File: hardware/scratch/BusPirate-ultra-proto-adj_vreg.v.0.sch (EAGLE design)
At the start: 18 parts, among them J1 CON_HEADER_1X02-PTH, J2 CON_HEADER_1X02-PTH, J3 CON_HEADER_1X02-PTH, Q1 DMMT3906W, Q3 FDS6575, U1 LM317T, U2 MCP6001

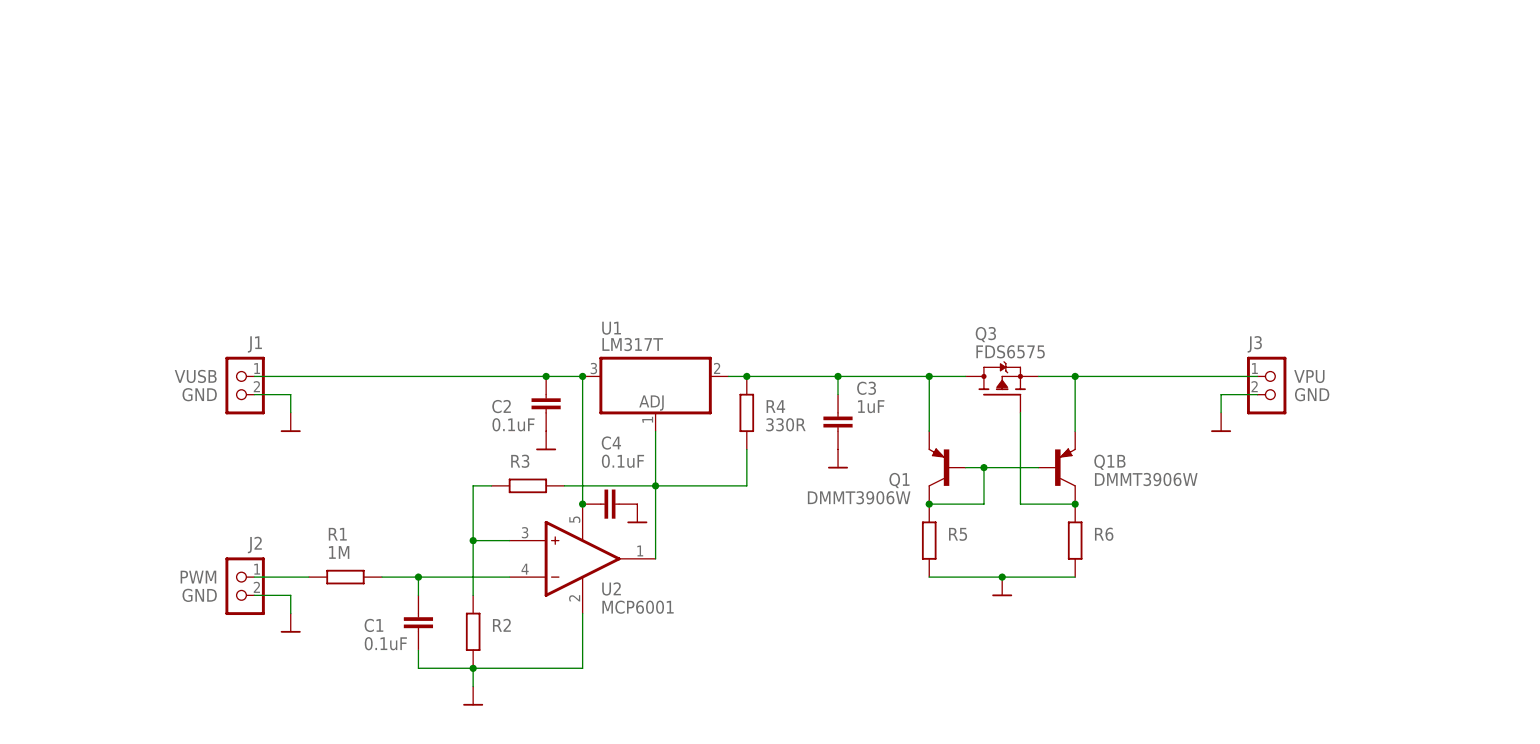
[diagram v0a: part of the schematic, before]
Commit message: changed vreg and pass mosfet
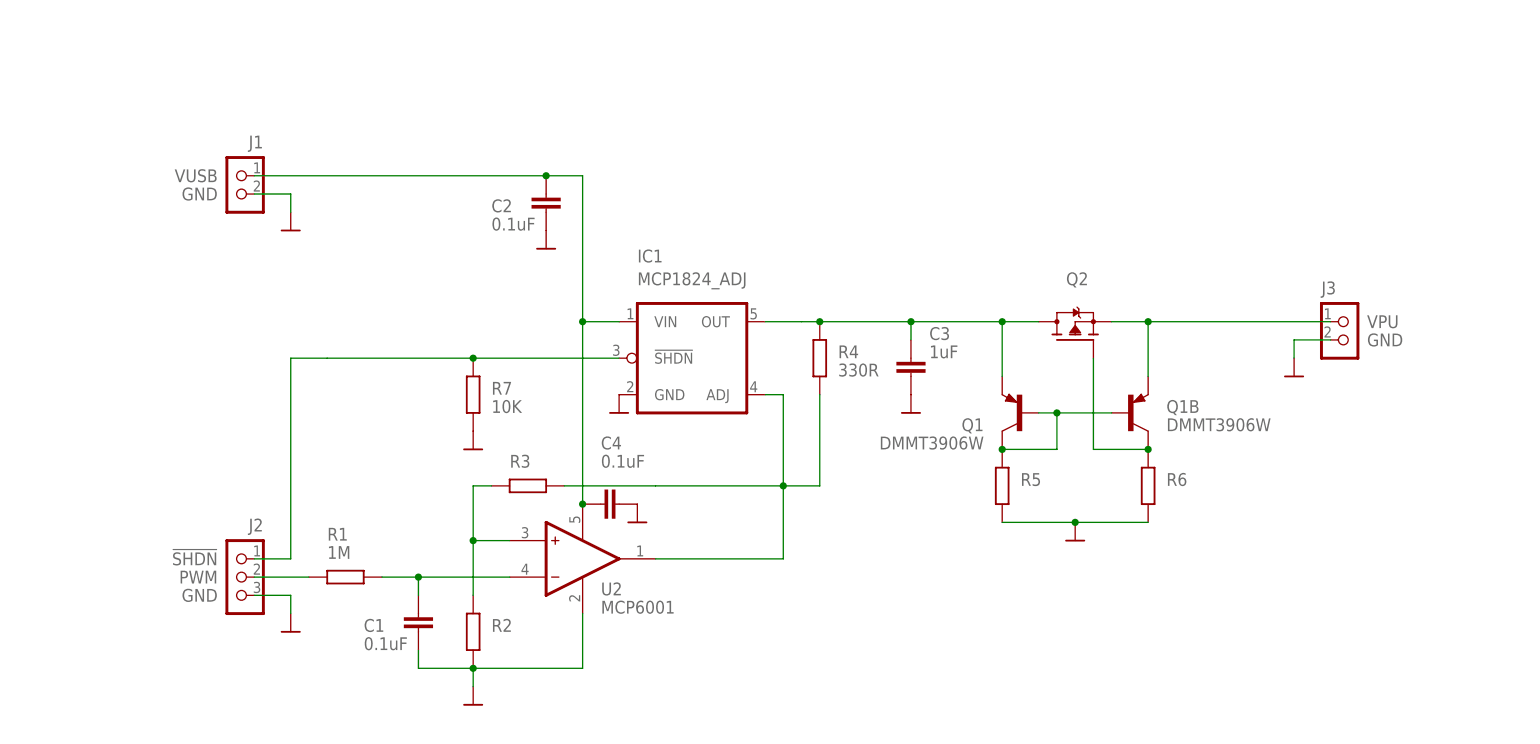
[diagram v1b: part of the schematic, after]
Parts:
- removed Q3: FDS6575, dp_devices.v6:TRANSISTOR-MOSFET-P_FDS6575
- removed U1: LM317T, dp_devices.v6:VREG_3PINS_ADJ-LM317T-D2PAK
- added IC1: MCP1824_ADJ, dp_devices.v6:IC_MCP1824_ADJ
- added Q2: (no value), dp_devices.v6:TRANSISTOR_FET_TSM2301CX
- added R7: 10K, dp_devices.v6:RESISTOR-0603
- J2: value CON_HEADER_1X02-PTH -> CON_HEADER_1X03-PTH; device dp_devices.v6:CON_HEADER_1X02-PTH -> dp_devices.v6:CON_HEADER_1X03-PTH
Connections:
- new net !SHDN: IC1.!SHDN, J2.1, R7.1
- net GND: now also IC1.GND, J2.3, R7.2; no longer J2.2
- net N$1: now also IC1.OUT, Q2.D; no longer Q3.D, U1.VOUT
- net N$4: now also Q2.G; no longer Q3.G
- net N$8: now also IC1.ADJ; no longer U1.ADJ
- net PWM: now also J2.2; no longer J2.1
- net VPU: now also Q2.S; no longer Q3.S
- net VUSB: now also IC1.VIN; no longer U1.VIN
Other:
- moved on the sheet: C2, C3, J1, J3, Q1, Q1B, R4, R5, R6
